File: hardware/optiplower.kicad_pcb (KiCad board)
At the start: 2 copper layers, 71.9 x 17.2 mm, 22 parts, among them J1 Conn_01x02, J2 Conn_01x03, U1 LR7533-M, U2 XL4015, U3 DS2502, U4 ATtiny25-20SSN, U5 ATtiny85-20PU, U6 DS2502S+

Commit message: Update part details
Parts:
- U4: value ATtiny25-20SSN -> ATtiny25-10SSU
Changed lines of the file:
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@@
     (descr "SOIC, 8 Pin (JEDEC MS-012AA, https://www.analog.com/media/en/package-pcb-resources/package/pkg_pdf/soic_narrow-r/r_8.pdf), generated with kicad-footprint-generator ipc_gullwing_generator.py")
     (tags "SOIC SO")
-    (property "Farnell PN" "2774976")
-    (property "LCSC" "C1339960")
-    (property "MPN" "ATtiny25-20SSN")
+    (property "Farnell PN" "1636952")
+    (property "LCSC" "C148097")
+    (property "MPN" "ATtiny25-10SSU")
     (property "Manufacturer" "Microchip")
     (property "Sheetfile" "optiplower.kicad_sch")
@@
         (effects (font (size 1 1) (thickness 0.15)))
     )
-    (fp_text value "ATtiny25-20SSN" (at 3.621 -4.191) (layer "F.Fab")
+    (fp_text value "ATtiny25-10SSU" (at 3.621 -4.191) (layer "F.Fab")
         (effects (font (size 1 1) (thickness 0.15)))
     )

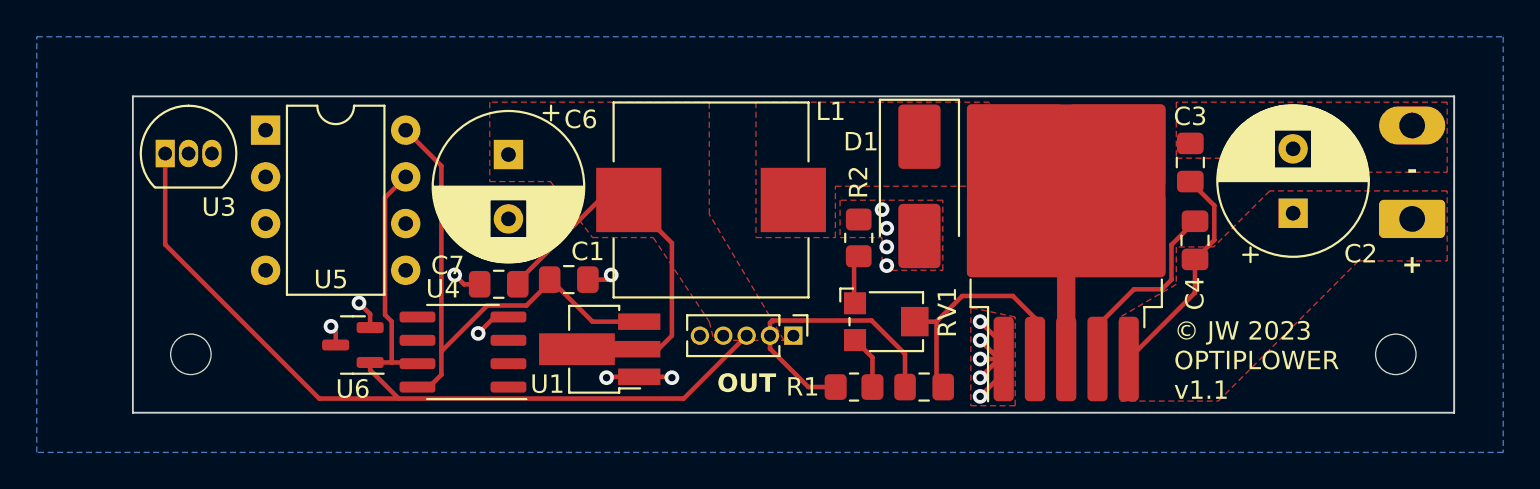
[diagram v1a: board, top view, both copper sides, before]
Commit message: Make design completely SMD
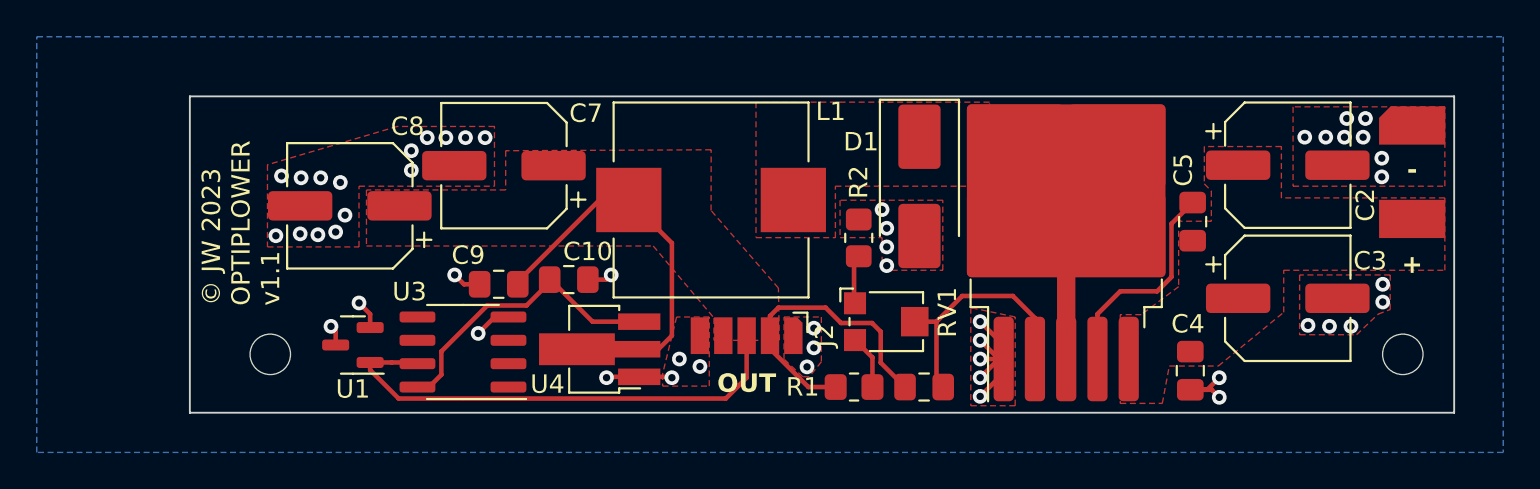
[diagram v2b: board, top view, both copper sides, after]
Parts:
- removed the C6 at (205.5, 81.6)
- removed the U3 at (186.8, 81.5)
- removed U5: ATtiny85-20PU, Package_DIP:DIP-8_W7.62mm
- added C3: 220uF, Capacitor_SMD:CP_Elec_6.3x7.7, F.Cu at (247.9, 89.4)
- added C7: 220uF, Capacitor_SMD:CP_Elec_6.3x7.7, F.Cu at (205.2, 82.2)
- added C8: 220uF, Capacitor_SMD:CP_Elec_6.3x7.7, F.Cu at (196.9, 84.4)
- C2: value 470uF -> 220uF; footprint Optiplower:CP_Radial_D8.0mm_P3.50mm_H11.5 -> Capacitor_SMD:CP_Elec_6.3x7.7
- J2: footprint Connector_PinHeader_1.27mm:PinHeader_1x05_P1.27mm_Vertical -> Optiplower:Output_pads
- moved C4 11.3 mm to (242.6, 93.3), turned to -90 degrees
- moved H1 4.32 mm to (192.5, 92.5)
- moved C2 2.63 mm to (247.9, 82.2), turned to 0 degrees
- moved C5 1.02 mm to (242.7, 85.2)
- moved H2 0.38 mm to (254.1, 92.5)
- renumbered C1 to C10, C3 to C4, C4 to C5, C5 to C6, C7 to C9, U6 to U1, U4 to U3, U1 to U4
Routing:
- net /SENSE: track 57.4 -> 26.9 mm
- net +3V3: track 29.1 -> 16.3 mm
- net +24V: track 12.1 -> 0.00 mm
- net GND: track 20.8 -> 24.4 mm, vias 16 -> 51
- net Net-(U2-VC): track 10.6 -> 11.8 mm
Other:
- board size 71.9 x 17.2 mm -> 68.8 x 17.2 mm
